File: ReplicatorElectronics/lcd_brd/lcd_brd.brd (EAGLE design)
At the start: 95.8 x 88.9 mm, 10 parts, among them J1 SBH11-PBPC-D17-ST-BK, J2 101-00708-64, U1 PETERATMEGA644_LCD37

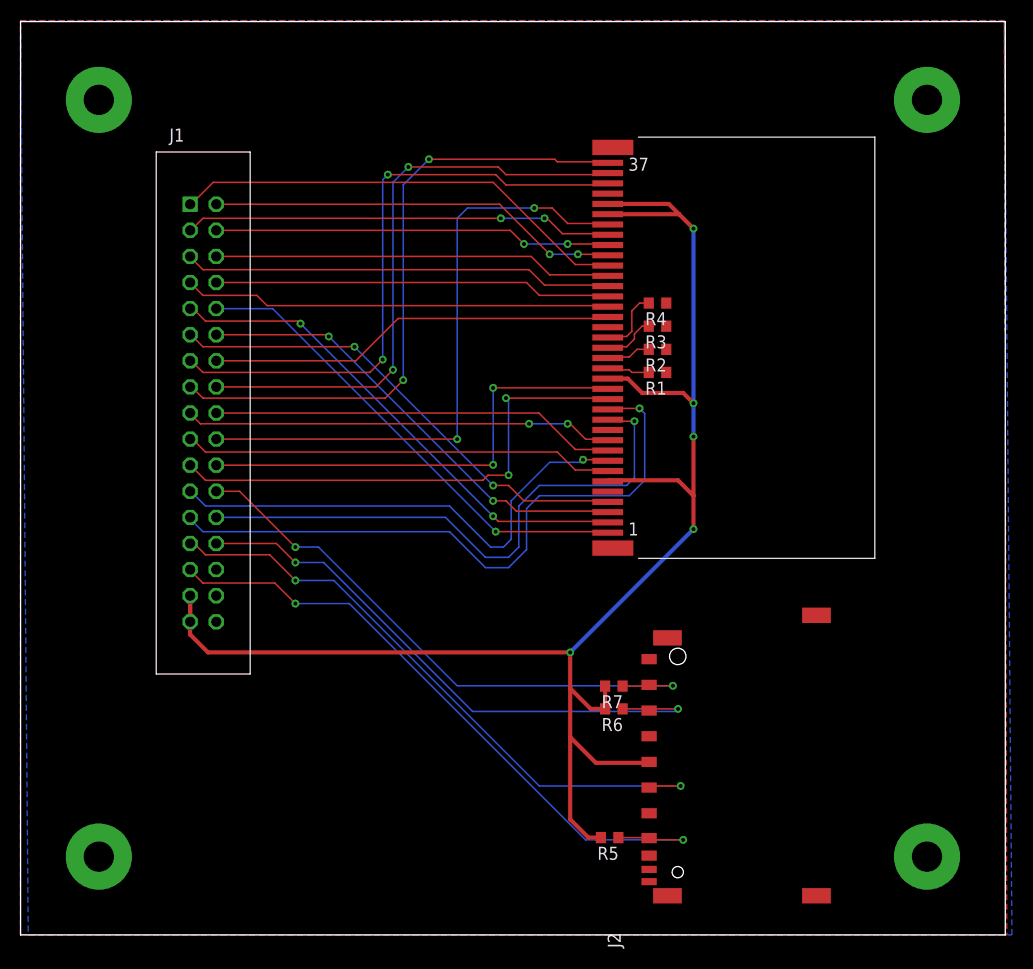
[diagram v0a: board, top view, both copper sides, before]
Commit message: 6/19/12: LCD Board layout complete with desired LCD footprint. DXF file updated.
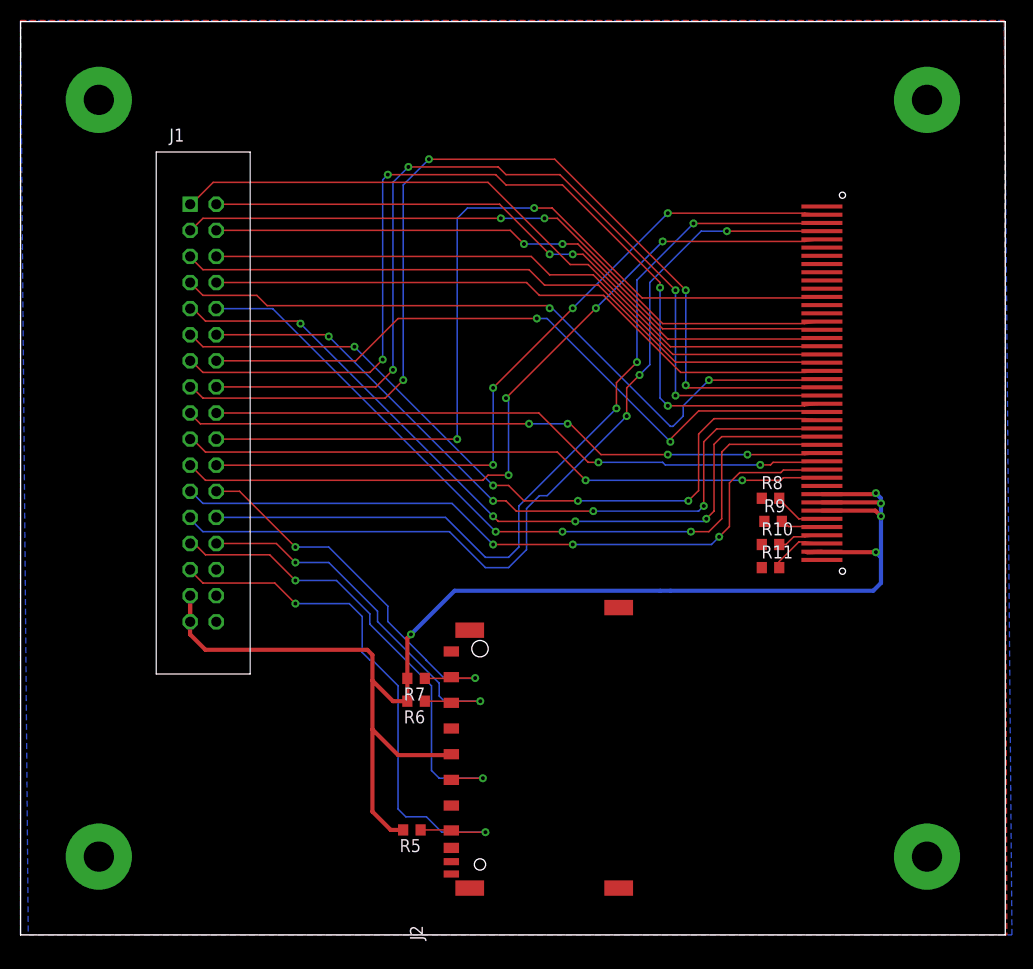
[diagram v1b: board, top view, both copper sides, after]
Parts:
- removed R1, R2, R3, R4: 22, resistor:R0603
- removed U1: PETERATMEGA644_LCD37, microtouch:PETERATMEGA644_LCD371MM
- added R10, R11, R8, R9: 22, resistor:R0603
- added U$1: ST2040Y3WY-RSLW-F, ST2040Y3WY-RSLW-F:ST0240Y3WY-RSLW-F
- moved J2 19.3 mm to (58.2, 4.56)
- moved R5 19.3 mm to (38.1, 10.2)
- moved R6 19.3 mm to (38.5, 22.8)
- moved R7 19.3 mm to (38.5, 25.0)
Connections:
- removed net N$1: R1.2, U1.17
- removed net N$3: R2.2, U1.18
- removed net N$4: R3.2, U1.19
- removed net N$6: R4.2, U1.20
- new net N$12: R8.2, U$1.39
- new net N$13: R9.2, U$1.40
- new net N$14: R10.2, U$1.41
- new net N$15: R11.2, U$1.42
- net A0: now also U$1.33; no longer U1.8
- net DB0: now also U$1.30; no longer U1.1
- net DB1: now also U$1.29; no longer U1.2
- net DB10: now also U$1.22; no longer U1.23
- net DB11: now also U$1.21; no longer U1.24
- net DB12: now also U$1.20; no longer U1.25
- net DB13: now also U$1.19; no longer U1.26
- net DB14: now also U$1.18; no longer U1.27
- net DB15: now also U$1.17; no longer U1.28
- net DB16: now also U$1.16; no longer U1.29
- net DB17: now also U$1.15; no longer U1.30
- net DB2: now also U$1.28; no longer U1.3
- net DB3: now also U$1.27; no longer U1.4
- net DB4: now also U$1.26; no longer U1.22
- net DB5: now also U$1.25; no longer U1.35
- net DB6: now also U$1.24; no longer U1.36
- net DB7: now also U$1.23; no longer U1.37
- net DGND: now also R10.1, R11.1, R8.1, R9.1, U$1.1, U$1.35, U$1.44, U$1.6, U$1.7, U$1.8; no longer R1.1, R2.1, R3.1, R4.1, U1.11, U1.21, U1.34, U1.5
- net LCD_CS: now also U$1.34; no longer U1.7
- net LCD_RD: now also U$1.31; no longer U1.10
- net LCD_RST: now also U$1.12; no longer U1.31
- net LCD_WR: now also U$1.32; no longer U1.9
- net VCC: now also U$1.36, U$1.37, U$1.38, U$1.43; no longer U1.16, U1.32, U1.33, U1.6
- net X+: now also U$1.3; no longer U1.12
- net X-: now also U$1.5; no longer U1.14
- net Y+: now also U$1.4; no longer U1.13
- net Y-: now also U$1.2; no longer U1.15
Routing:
- net DB5: track 59.8 -> 96.1 mm, vias 2 -> 4
- net DB6: track 58.0 -> 93.7 mm, vias 2 -> 4
- net DB7: track 62.0 -> 97.3 mm, vias 2 -> 4
- net DB0: track 47.1 -> 75.3 mm, vias 1 -> 3
- net DB10: track 41.6 -> 69.7 mm, vias 0 -> 2
- net DB1: track 49.3 -> 77.3 mm, vias 2 -> 4
- net Y-: track 45.7 -> 73.5 mm, vias 2 -> 4
- net DB2: track 45.3 -> 73.0 mm, vias 2 -> 4
- net DB3: track 47.4 -> 74.7 mm, vias 2 -> 4
- net DB4: track 39.9 -> 67.0 mm, vias 0 -> 2
- net X-: track 49.4 -> 76.5 mm, vias 2 -> 4
- net X+: track 56.2 -> 82.5 mm, vias 1 -> 3
- net DB17: track 41.8 -> 66.2 mm
- net DB15: track 40.2 -> 64.4 mm
- net DB16: track 38.7 -> 62.9 mm
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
